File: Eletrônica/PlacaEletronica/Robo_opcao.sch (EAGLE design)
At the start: 111 parts, among them J1 PJ-002A, J3 ZX62-B-5PA, J4 F-1X06-SIP-100-40, Q1 SMD-TRANSISTORS-NPN-25V-500MW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, Q2 SMD-TRANSISTORS-NPN-25V-500MW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, Q4 SFH_3716, Q5 TSOP4838, U1 ESP32-WROOM-32D, U2 AMS1117-3.3, U3 INTERFACE-CP2102-GMR(QFN28)QF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

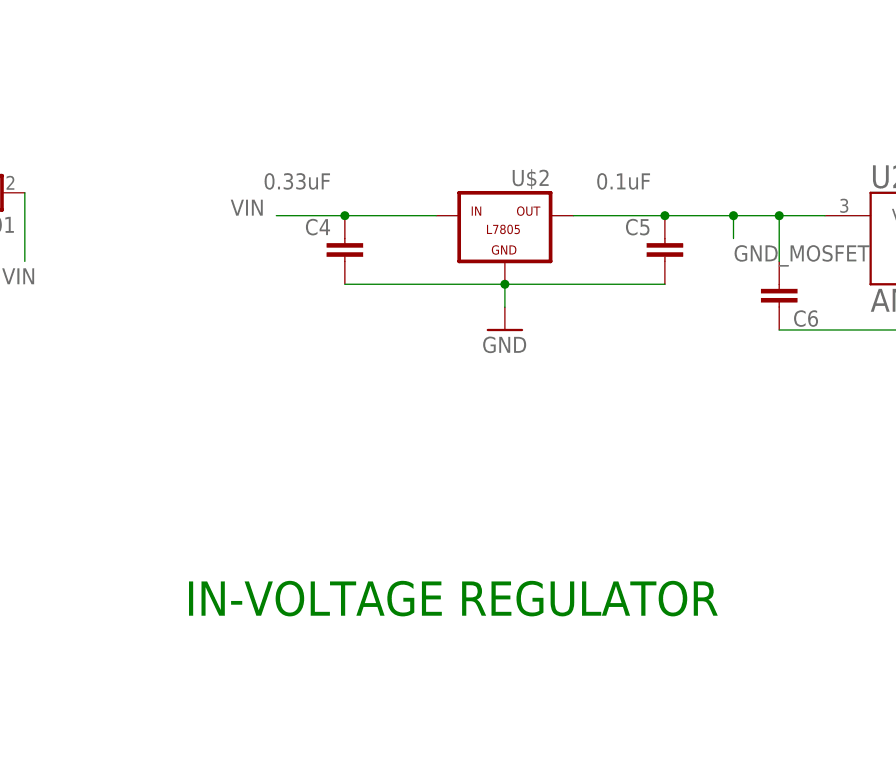
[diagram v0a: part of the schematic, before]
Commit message: [MODIFIED] Regulador de tensao em paralelo
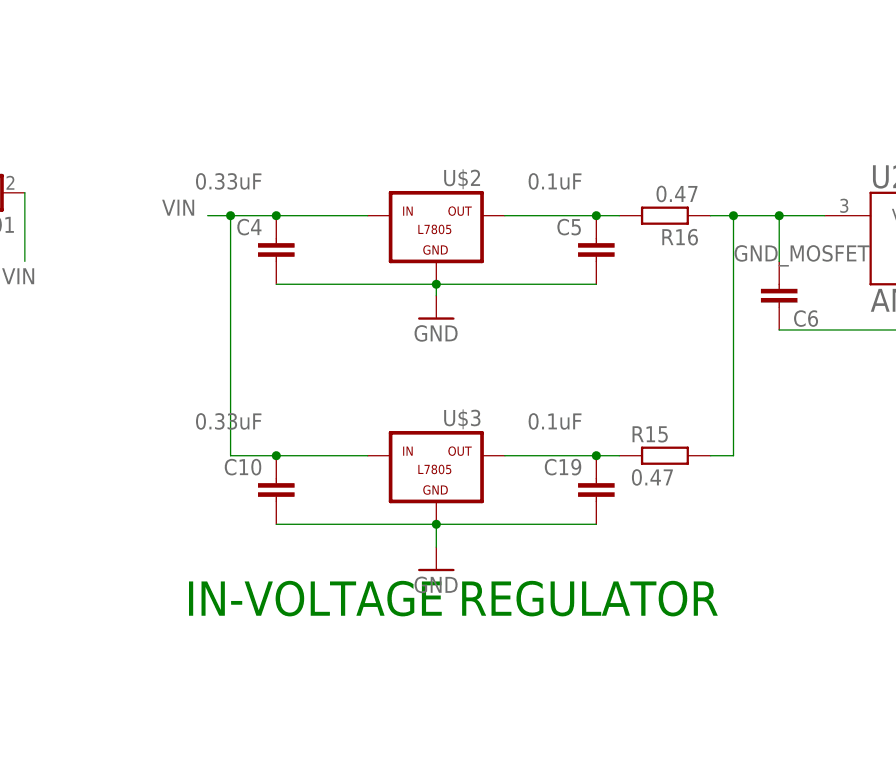
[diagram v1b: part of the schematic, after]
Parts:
- added C10: 0.33uF, Perfect_0402:CAP_0402
- added C19: 0.1uF, Perfect_0402:CAP_0402
- added R15, R16: 0.47, rcl:R-EU_M0805
- added U$3: -L7805, tango:-L7805
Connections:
- new net N$1: C19.2, R15.1, U$3.OUT
- new net N$2: C5.2, R16.2, U$2.OUT
- net GND: now also C10.1, C19.1, U$3.GND
- net GND_MOSFET: now also R15.2, R16.1; no longer C5.2, U$2.OUT
- net VIN: now also C10.2, U$3.IN
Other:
- moved on the sheet: C4, C5, U$2
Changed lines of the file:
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@@
 <part name="U$2" library="tango" deviceset="-L7805" device=""/>
 <part name="S6" library="switch" library_urn="urn:adsk.eagle:library:380" deviceset="255SB" device="" package3d_urn="urn:adsk.eagle:package:27679/1"/>
+<part name="GND2" library="supply1" library_urn="urn:adsk.eagle:library:371" deviceset="GND" device=""/>
+<part name="C10" library="Perfect_0402" deviceset="CAP_0402" device="" value="0.33uF"/>
+<part name="C19" library="Perfect_0402" deviceset="CAP_0402" device="" value="0.1uF"/>
+<part name="U$3" library="tango" deviceset="-L7805" device=""/>
+<part name="R15" library="rcl" library_urn="urn:adsk.eagle:library:334" deviceset="R-EU_" device="M0805" package3d_urn="urn:adsk.eagle:package:23556/2" value="0.47"/>
+<part name="R16" library="rcl" library_urn="urn:adsk.eagle:library:334" deviceset="R-EU_" device="M0805" package3d_urn="urn:adsk.eagle:package:23556/2" value="0.47"/>
 </parts>
 <sheets>
@@
 </plain>
 <instances>
-<instance part="GND6" gate="1" x="121.92" y="45.72" smashed="yes">
-<attribute name="VALUE" x="119.38" y="43.18" size="1.778" layer="96"/>
-</instance>
-<instance part="C4" gate="G$1" x="104.14" y="58.42" smashed="yes" rot="R180">
-<attribute name="NAME" x="102.616" y="58.039" size="1.778" layer="95" rot="R180"/>
-<attribute name="VALUE" x="102.616" y="63.119" size="1.778" layer="96" rot="R180"/>
-</instance>
-<instance part="C5" gate="G$1" x="139.7" y="58.42" smashed="yes" rot="R180">
-<attribute name="NAME" x="138.176" y="58.039" size="1.778" layer="95" rot="R180"/>
-<attribute name="VALUE" x="138.176" y="63.119" size="1.778" layer="96" rot="R180"/>
+<instance part="GND6" gate="1" x="114.3" y="46.99" smashed="yes">
+<attribute name="VALUE" x="111.76" y="44.45" size="1.778" layer="96"/>
+</instance>
+<instance part="C4" gate="G$1" x="96.52" y="58.42" smashed="yes" rot="R180">
+<attribute name="NAME" x="94.996" y="58.039" size="1.778" layer="95" rot="R180"/>
+<attribute name="VALUE" x="94.996" y="63.119" size="1.778" layer="96" rot="R180"/>
+</instance>
+<instance part="C5" gate="G$1" x="132.08" y="58.42" smashed="yes" rot="R180">
+<attribute name="NAME" x="130.556" y="58.039" size="1.778" layer="95" rot="R180"/>
+<attribute name="VALUE" x="130.556" y="63.119" size="1.778" layer="96" rot="R180"/>
 </instance>
 <instance part="U1" gate="G$1" x="71.12" y="144.78" smashed="yes">
@@
 <attribute name="VALUE" x="576.58" y="182.88" size="1.778" layer="96" rot="R180"/>
 </instance>
-<instance part="U$2" gate="G$1" x="121.92" y="55.88" smashed="yes">
-<attribute name="NAME" x="127" y="63.5" size="1.778" layer="95" rot="R180"/>
+<instance part="U$2" gate="G$1" x="114.3" y="55.88" smashed="yes">
+<attribute name="NAME" x="119.38" y="63.5" size="1.778" layer="95" rot="R180"/>
 </instance>
 <instance part="S6" gate="1" x="511.81" y="19.05" smashed="yes" rot="R270">
 <attribute name="NAME" x="509.905" y="25.4" size="1.778" layer="95"/>
 <attribute name="VALUE" x="514.985" y="22.86" size="1.778" layer="96"/>
+</instance>
+<instance part="GND2" gate="1" x="114.3" y="19.05" smashed="yes">
+<attribute name="VALUE" x="111.76" y="16.51" size="1.778" layer="96"/>
+</instance>
+<instance part="C10" gate="G$1" x="96.52" y="31.75" smashed="yes" rot="R180">
+<attribute name="NAME" x="94.996" y="31.369" size="1.778" layer="95" rot="R180"/>
+<attribute name="VALUE" x="94.996" y="36.449" size="1.778" layer="96" rot="R180"/>
+</instance>
+<instance part="C19" gate="G$1" x="132.08" y="31.75" smashed="yes" rot="R180">
+<attribute name="NAME" x="130.556" y="31.369" size="1.778" layer="95" rot="R180"/>
+<attribute name="VALUE" x="130.556" y="36.449" size="1.778" layer="96" rot="R180"/>
+</instance>
+<instance part="U$3" gate="G$1" x="114.3" y="29.21" smashed="yes">
+<attribute name="NAME" x="119.38" y="36.83" size="1.778" layer="95" rot="R180"/>
+</instance>
+<instance part="R15" gate="G$1" x="139.7" y="31.75" smashed="yes">
+<attribute name="NAME" x="135.89" y="33.2486" size="1.778" layer="95"/>
+<attribute name="VALUE" x="135.89" y="28.448" size="1.778" layer="96"/>
+</instance>
+<instance part="R16" gate="G$1" x="139.7" y="58.42" smashed="yes" rot="R180">
+<attribute name="NAME" x="143.51" y="56.9214" size="1.778" layer="95" rot="R180"/>
+<attribute name="VALUE" x="143.51" y="61.722" size="1.778" layer="96" rot="R180"/>
 </instance>
 </instances>
@@
 <pinref part="U$2" gate="G$1" pin="GND"/>
 <pinref part="GND6" gate="1" pin="GND"/>
-<wire x1="121.92" y1="50.8" x2="121.92" y2="48.26" width="0.1524" layer="91"/>
+<wire x1="114.3" y1="50.8" x2="114.3" y2="49.53" width="0.1524" layer="91"/>
 <pinref part="C4" gate="G$1" pin="1"/>
 <pinref part="C5" gate="G$1" pin="1"/>
-<wire x1="104.14" y1="50.8" x2="121.92" y2="50.8" width="0.1524" layer="91"/>
-<junction x="121.92" y="50.8"/>
-<wire x1="121.92" y1="50.8" x2="139.7" y2="50.8" width="0.1524" layer="91"/>
+<wire x1="96.52" y1="50.8" x2="114.3" y2="50.8" width="0.1524" layer="91"/>
+<junction x="114.3" y="50.8"/>
+<wire x1="114.3" y1="50.8" x2="132.08" y2="50.8" width="0.1524" layer="91"/>
+</segment>
+<segment>
+<pinref part="U$3" gate="G$1" pin="GND"/>
+<pinref part="GND2" gate="1" pin="GND"/>
+<wire x1="114.3" y1="24.13" x2="114.3" y2="21.59" width="0.1524" layer="91"/>
+<pinref part="C10" gate="G$1" pin="1"/>
+<pinref part="C19" gate="G$1" pin="1"/>
+<wire x1="96.52" y1="24.13" x2="114.3" y2="24.13" width="0.1524" layer="91"/>
+<junction x="114.3" y="24.13"/>
+<wire x1="114.3" y1="24.13" x2="132.08" y2="24.13" width="0.1524" layer="91"/>
 </segment>
 </net>
@@
 <net name="VIN" class="0">
 <segment>
-<pinref part="C4" gate="G$1" pin="2"/>
-<wire x1="104.14" y1="58.42" x2="96.52" y2="58.42" width="0.1524" layer="91"/>
-<label x="91.44" y="58.42" size="1.778" layer="95"/>
-<wire x1="104.14" y1="58.42" x2="114.3" y2="58.42" width="0.1524" layer="91"/>
-<junction x="104.14" y="58.42"/>
-<pinref part="U$2" gate="G$1" pin="IN"/>
-</segment>
-<segment>
 <label x="66.04" y="50.8" size="1.778" layer="95"/>
 <wire x1="68.58" y1="60.96" x2="68.58" y2="53.34" width="0.1524" layer="91"/>
@@
 <wire x1="553.72" y1="224.79" x2="552.45" y2="224.79" width="0.1524" layer="91"/>
 <label x="552.45" y="226.06" size="1.778" layer="95" rot="R180"/>
+</segment>
+<segment>
+<pinref part="C10" gate="G$1" pin="2"/>
+<wire x1="96.52" y1="31.75" x2="106.68" y2="31.75" width="0.1524" layer="91"/>
+<pinref part="U$3" gate="G$1" pin="IN"/>
+<pinref part="C4" gate="G$1" pin="2"/>
+<wire x1="96.52" y1="58.42" x2="91.44" y2="58.42" width="0.1524" layer="91"/>
+<label x="83.82" y="58.42" size="1.778" layer="95"/>
+<wire x1="91.44" y1="58.42" x2="88.9" y2="58.42" width="0.1524" layer="91"/>
+<wire x1="96.52" y1="58.42" x2="106.68" y2="58.42" width="0.1524" layer="91"/>
+<junction x="96.52" y="58.42"/>
+<pinref part="U$2" gate="G$1" pin="IN"/>
+<wire x1="96.52" y1="31.75" x2="91.44" y2="31.75" width="0.1524" layer="91"/>
+<wire x1="91.44" y1="31.75" x2="91.44" y2="58.42" width="0.1524" layer="91"/>
+<junction x="96.52" y="31.75"/>
+<junction x="91.44" y="58.42"/>
 </segment>
 </net>
@@
 </segment>
 <segment>
-<wire x1="147.32" y1="58.42" x2="147.32" y2="55.88" width="0.1524" layer="91"/>
-<label x="147.32" y="53.34" size="1.778" layer="95"/>
-<pinref part="C5" gate="G$1" pin="2"/>
-<wire x1="129.54" y1="58.42" x2="139.7" y2="58.42" width="0.1524" layer="91"/>
-<wire x1="139.7" y1="58.42" x2="147.32" y2="58.42" width="0.1524" layer="91"/>
-<junction x="139.7" y="58.42"/>
-<pinref part="U2" gate="G$1" pin="VIN"/>
-<wire x1="147.32" y1="58.42" x2="152.4" y2="58.42" width="0.1524" layer="91"/>
-<junction x="147.32" y="58.42"/>
-<pinref part="C6" gate="G$1" pin="1"/>
-<wire x1="152.4" y1="58.42" x2="157.48" y2="58.42" width="0.1524" layer="91"/>
-<wire x1="152.4" y1="53.34" x2="152.4" y2="58.42" width="0.1524" layer="91"/>
-<junction x="152.4" y="58.42"/>
-<pinref part="U$2" gate="G$1" pin="OUT"/>
-</segment>
-<segment>
 <pinref part="D10" gate="1" pin="C"/>
 <wire x1="342.9" y1="204.47" x2="342.9" y2="207.01" width="0.1524" layer="91"/>
@@
 <junction x="422.91" y="31.75"/>
 </segment>
+<segment>
+<label x="147.32" y="53.34" size="1.778" layer="95"/>
+<pinref part="U2" gate="G$1" pin="VIN"/>
+<wire x1="147.32" y1="58.42" x2="152.4" y2="58.42" width="0.1524" layer="91"/>
+<pinref part="C6" gate="G$1" pin="1"/>
+<wire x1="152.4" y1="58.42" x2="157.48" y2="58.42" width="0.1524" layer="91"/>
+<wire x1="152.4" y1="53.34" x2="152.4" y2="58.42" width="0.1524" layer="91"/>
+<junction x="152.4" y="58.42"/>
+<pinref part="R16" gate="G$1" pin="1"/>
+<wire x1="144.78" y1="58.42" x2="147.32" y2="58.42" width="0.1524" layer="91"/>
+<junction x="147.32" y="58.42"/>
+<pinref part="R15" gate="G$1" pin="2"/>
+<wire x1="144.78" y1="31.75" x2="147.32" y2="31.75" width="0.1524" layer="91"/>
+<wire x1="147.32" y1="31.75" x2="147.32" y2="58.42" width="0.1524" layer="91"/>
+</segment>
 </net>
 <net name="N$28" class="0">
@@
 </segment>
 </net>
+<net name="N$1" class="0">
+<segment>
+<pinref part="C19" gate="G$1" pin="2"/>
+<wire x1="121.92" y1="31.75" x2="132.08" y2="31.75" width="0.1524" layer="91"/>
+<pinref part="U$3" gate="G$1" pin="OUT"/>
+<pinref part="R15" gate="G$1" pin="1"/>
+<wire x1="132.08" y1="31.75" x2="134.62" y2="31.75" width="0.1524" layer="91"/>
+<junction x="132.08" y="31.75"/>
+</segment>
+</net>
+<net name="N$2" class="0">
+<segment>
+<pinref part="C5" gate="G$1" pin="2"/>
+<wire x1="121.92" y1="58.42" x2="132.08" y2="58.42" width="0.1524" layer="91"/>
+<pinref part="U$2" gate="G$1" pin="OUT"/>
+<pinref part="R16" gate="G$1" pin="2"/>
+<wire x1="132.08" y1="58.42" x2="134.62" y2="58.42" width="0.1524" layer="91"/>
+<junction x="132.08" y="58.42"/>
+</segment>
+</net>

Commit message: [MODIFIED] Pinos do Engino
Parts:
- removed JP2: (no value), pinhead-1:PINHD-1X1_2.54-SMD
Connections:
- removed net GND_MOSFET: C34.2, C35.+, C36.2, C37.+, C38.2, C39.+, C40.2, C41.+, C42.2, C43.+, C44.2, C45.+, C46.2, C47.+, C48.2, C49.+, C6.1, D10.C, D11.C, D12.C, D13.C, D14.C, D15.C, D16.C, D17.C, JP2.1, JP4.4, JP9.5, R15.2, R16.1, U2.VIN, V3/+UB.+UB, V4/+UB.+UB
- new net GND_MOSFET~5V: C34.2, C35.+, C36.2, C37.+, C38.2, C39.+, C40.2, C41.+, C42.2, C43.+, C44.2, C45.+, C46.2, C47.+, C48.2, C49.+, C6.1, D10.C, D11.C, D12.C, D13.C, D14.C, D15.C, D16.C, D17.C, JP4.4, JP9.5, R15.2, R16.1, U2.VIN, V3/+UB.+UB, V4/+UB.+UB
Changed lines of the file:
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@@
 <part name="R14" library="rcl" library_urn="urn:adsk.eagle:library:334" deviceset="R-EU_" device="M0805" package3d_urn="urn:adsk.eagle:package:23556/2" value="220"/>
 <part name="GND11" library="supply1" library_urn="urn:adsk.eagle:library:371" deviceset="GND" device=""/>
-<part name="JP2" library="pinhead-1" deviceset="PINHD-1X1" device="_2.54-SMD"/>
 <part name="U$2" library="tango" deviceset="-L7805" device=""/>
 <part name="S6" library="switch" library_urn="urn:adsk.eagle:library:380" deviceset="255SB" device="" package3d_urn="urn:adsk.eagle:package:27679/1"/>
@@
 <attribute name="VALUE" x="364.49" y="-71.12" size="1.778" layer="96"/>
 </instance>
-<instance part="JP2" gate="G$1" x="570.23" y="177.8" smashed="yes" rot="R180">
-<attribute name="NAME" x="576.58" y="174.625" size="1.778" layer="95" rot="R180"/>
-<attribute name="VALUE" x="576.58" y="182.88" size="1.778" layer="96" rot="R180"/>
-</instance>
 <instance part="U$2" gate="G$1" x="114.3" y="55.88" smashed="yes">
 <attribute name="NAME" x="119.38" y="63.5" size="1.778" layer="95" rot="R180"/>
@@
 </segment>
 </net>
-<net name="GND_MOSFET" class="0">
+<net name="GND_MOSFET~5V" class="0">
 <segment>
 <pinref part="V3" gate="/+UB" pin="+UB"/>
@@
 </segment>
 <segment>
-<pinref part="JP2" gate="G$1" pin="1"/>
-<wire x1="572.77" y1="177.8" x2="579.12" y2="177.8" width="0.1524" layer="91"/>
-<label x="579.12" y="177.8" size="1.778" layer="95"/>
-</segment>
-<segment>
